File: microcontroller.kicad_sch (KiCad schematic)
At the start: 27 parts, among them J7 Conn_02x10_Odd_Even, J8 Conn_ST_STDC14, Q8 NPN, Q9 NMOS, SW1 SW_Push, U10 MCP9808T-E/MS, U2 STM32G491KEU6

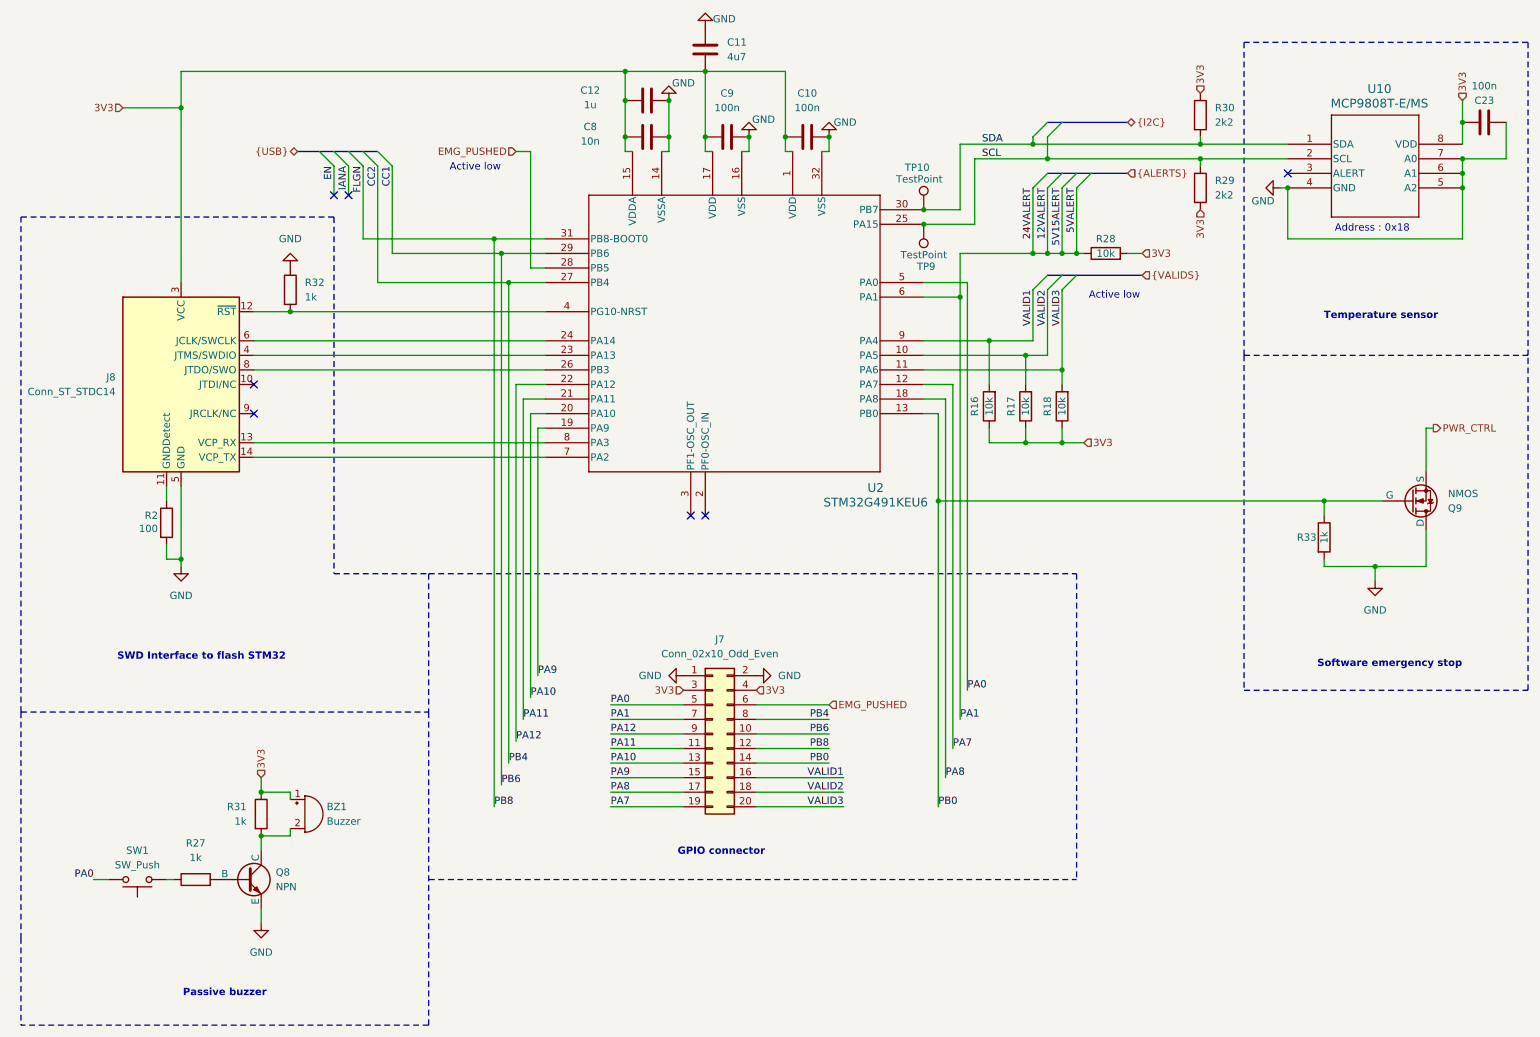
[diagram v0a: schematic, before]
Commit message: Correctifs et améliorations + passage à KiCad V9
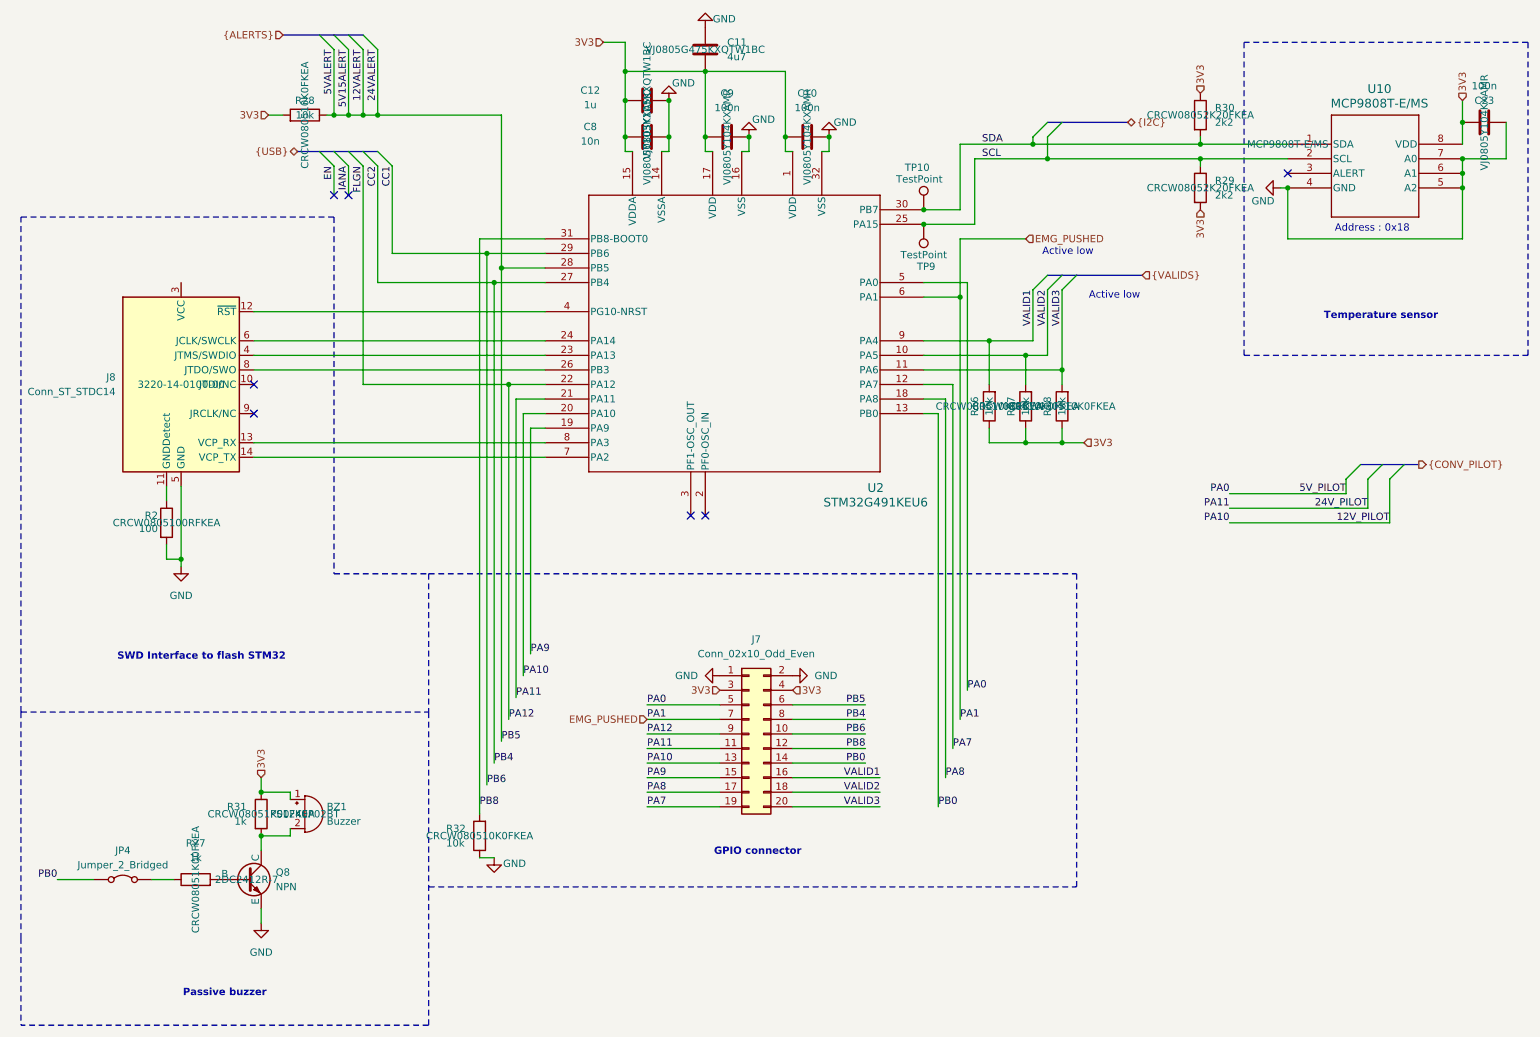
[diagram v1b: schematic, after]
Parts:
- removed Q9: NMOS, Package_TO_SOT_SMD:SOT-23, symbol Simulation_SPICE:NMOS
- removed R33: 1k, Resistor_SMD:R_0805_2012Metric_Pad1.20x1.40mm_HandSolder, symbol Device:R
- removed SW1: SW_Push, Modelec:SW_DS01-254-L-01BE_CUD, symbol Switch:SW_Push
- added JP4: Jumper_2_Bridged, Connector_PinHeader_1.27mm:PinHeader_1x02_P1.27mm_Vertical, symbol Jumper:Jumper_2_Bridged
- BZ1: Manufacturer_Part_Number (none) -> PS1240P02BT
- C10, C23, C9: Manufacturer_Part_Number (none) -> VJ0805Y104KXAMR
- C11: Manufacturer_Part_Number (none) -> VJ0805G475KXQTW1BC
- C12: Manufacturer_Part_Number (none) -> VJ0805Y105KXQTW1BC
- C8: Manufacturer_Part_Number (none) -> VJ0805Y103KXAMC
- J8: Manufacturer_Part_Number (none) -> 3220-14-0100-00
- Q8: Manufacturer_Part_Number (none) -> 2DC2412R-7
- R16, R17, R18, R28: Manufacturer_Part_Number (none) -> CRCW080510K0FKEA
- R2: Manufacturer_Part_Number (none) -> CRCW0805100RFKEA
- R27, R31: Manufacturer_Part_Number (none) -> CRCW08051K00FKEA
- R29, R30: Manufacturer_Part_Number (none) -> CRCW08052K20FKEA
- R32: value 1k -> 10k; Manufacturer_Part_Number (none) -> CRCW080510K0FKEA
- U10: Manufacturer_Part_Number (none) -> MCP9808T-E/MS
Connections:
- net PA12 is gone; now on net FLGN: J7.9 (Pin_9), U2.22 (PA12)
- net 12VALERT: now also J7.6 (Pin_6), U2.28 (PB5); no longer J7.7 (Pin_7), U2.6 (PA1)
- net 3V3: no longer J8.3 (VCC)
- net EMG_PUSHED: now also J7.7 (Pin_7), U2.6 (PA1); no longer J7.6 (Pin_6), U2.28 (PB5)
- net FLGN: no longer J7.12 (Pin_12), U2.31 (PB8-BOOT0)
- net PB0: now also JP4.1 (A)
- net at R27.1: now also JP4.2 (B)
- net at J8.12 (~{RST}), U2.4 (PG10-NRST): no longer R32.2
- net PA0 renamed 5V_PILOT
- net PA10 renamed 12V_PILOT
- net PA11 renamed 24V_PILOT
- new net PB8: J7.12 (Pin_12), R32.2, U2.31 (PB8-BOOT0)
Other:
- note removed: "Software emergency stop"
- moved on the sheet: J7
